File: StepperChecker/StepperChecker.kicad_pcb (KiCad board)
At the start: 2 copper layers, 89.4 x 69.1 mm, 31 parts, among them CN5 FEMALE_LEFT, CN6 FEMALE_RIGHT, J1 PJ-202AH, J10 CFG2, J11 CFG3, J12 Terminal, J2 Terminal, J3 FEATHER_A, J4 Molex SL, J5 JST-XH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

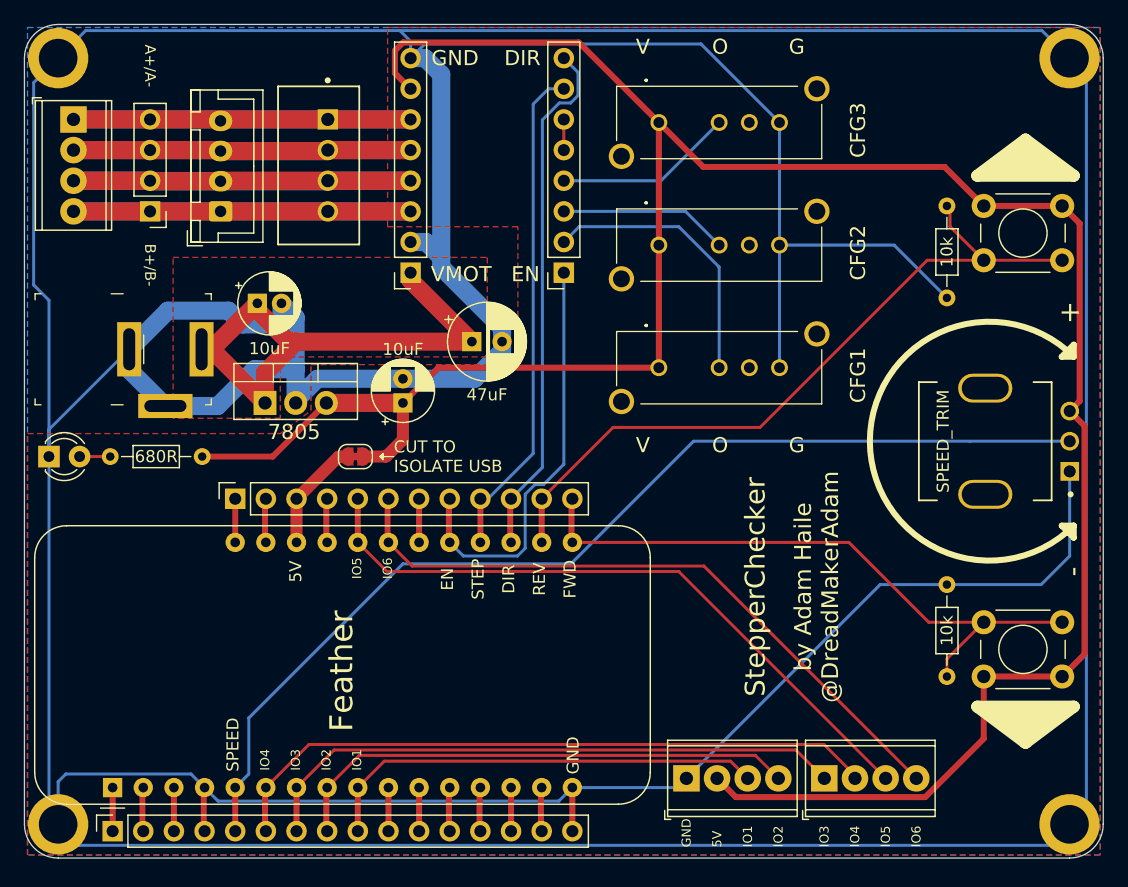
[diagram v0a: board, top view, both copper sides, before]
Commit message: Add Recom and jumpers
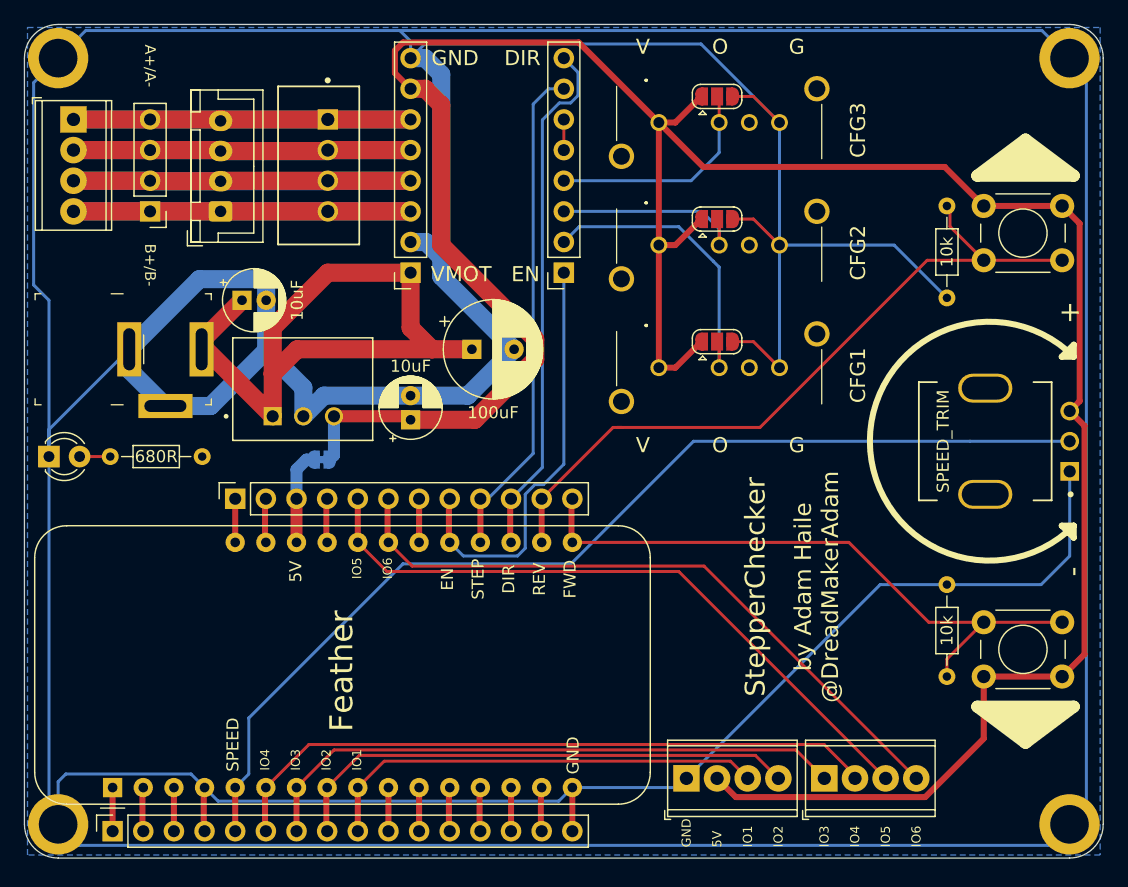
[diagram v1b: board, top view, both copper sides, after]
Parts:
- added JP1: CFG1, Jumper:SolderJumper-3_P1.3mm_Open_RoundedPad1.0x1.5mm, F.Cu at (152.4, 61.6)
- added JP3: CFG2, Jumper:SolderJumper-3_P1.3mm_Open_RoundedPad1.0x1.5mm, F.Cu at (152.4, 51.4)
- added JP4: CFG3, Jumper:SolderJumper-3_P1.3mm_Open_RoundedPad1.0x1.5mm, F.Cu at (152.4, 41.3)
- C3: value 47uF -> 100uF; footprint Capacitor_THT:CP_Radial_D6.3mm_P2.50mm -> Capacitor_THT:CP_Radial_D8.0mm_P3.50mm
- JP2: moved to B.Cu
- U2: value LM7805_TO220 -> R-78E5.0-1.0; footprint Package_TO_SOT_THT:TO-220-3_Vertical -> R-78E5.0-1:CONV_R-78E5.0-1.0
- moved U2 3.37 mm to (118.1, 65.5)
- moved JP2 2.81 mm to (119.6, 71.4)
- moved C2 1.53 mm to (127.0, 68.1)
- moved C1 1.30 mm to (113.0, 58.2)
- moved C3 0.63 mm to (132.1, 62.2)
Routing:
- net 5V: track 210.6 -> 226.1 mm
- net GND: track 589.0 -> 604.0 mm
- net VIN: track 45.9 -> 58.7 mm
- net /StepDriverX/CFG3: track 14.9 -> 18.6 mm
- net /StepDriverX/CFG2: track 14.0 -> 17.1 mm
- net /StepDriverX/CFG1: track 23.1 -> 25.4 mm
- net Net-(J8-Pad3): track 12.5 -> 11.0 mm
- removed copper zone on F.Cu, net 5V
- removed copper zone on F.Cu, net VIN
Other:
- board text removed: "7805"

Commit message: Fix missing traces and fill
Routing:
- net 5V: track 226.1 -> 240.0 mm
- added copper zone on F.Cu, net 5V
- added copper zone on F.Cu, net VIN
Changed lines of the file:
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@@
     (thickness 1.6)
     (drawings 99)
-    (tracks 306)
+    (tracks 309)
     (zones 0)
     (modules 34)
@@
   (page A4)
   (layers
-    (0 F.Cu signal)
-    (31 B.Cu signal)
+    (0 F.Cu signal hide)
+    (31 B.Cu signal hide)
     (32 B.Adhes user)
     (33 F.Adhes user)
@@
   (segment (start 148.941 63.754) (end 151.1 61.595) (width 0.5) (layer F.Cu) (net 2))
   (segment (start 147.574 63.754) (end 148.941 63.754) (width 0.5) (layer F.Cu) (net 2))
+  (segment (start 109.728 71.12) (end 120.015 71.12) (width 0.5) (layer F.Cu) (net 2))
+  (segment (start 120.65 70.485) (end 120.65 67.782) (width 0.5) (layer F.Cu) (net 2))
+  (segment (start 120.015 71.12) (end 120.65 70.485) (width 0.5) (layer F.Cu) (net 2))
   (segment (start 152.574 61.769) (end 152.4 61.595) (width 0.25) (layer F.Cu) (net 3))
   (segment (start 152.574 63.754) (end 152.574 61.769) (width 0.25) (layer F.Cu) (net 3))
@@
     (connect_pads (clearance 0.508))
     (min_thickness 0.254)
-    (fill (arc_segments 32) (thermal_gap 0.508) (thermal_bridge_width 0.508))
+    (fill yes (arc_segments 32) (thermal_gap 0.508) (thermal_bridge_width 0.508))
     (polygon
       (pts
@@
       )
     )
+  )
+  (zone (net 8) (net_name VIN) (layer F.Cu) (hatch edge 0.508)
+    (connect_pads (clearance 0.508))
+    (min_thickness 0.254)
+    (fill yes (arc_segments 32) (thermal_gap 0.508) (thermal_bridge_width 0.508))
+    (polygon
+      (pts
+        (xy 133.985 64.77) (xy 116.84 64.77) (xy 116.84 69.215) (xy 106.68 69.215) (xy 106.68 54.61)
+        (xy 133.985 54.61)
+      )
+    )
+  )
+  (zone (net 2) (net_name 5V) (layer F.Cu) (hatch edge 0.508)
+    (connect_pads (clearance 0.508))
+    (min_thickness 0.254)
+    (fill yes (arc_segments 32) (thermal_gap 0.508) (thermal_bridge_width 0.508))
+    (polygon
+      (pts
+        (xy 184.15 104.14) (xy 95.25 104.775) (xy 95.25 69.85) (xy 119.38 69.85) (xy 119.38 66.04)
+        (xy 135.255 66.04) (xy 135.255 53.34) (xy 124.46 53.34) (xy 124.46 35.56) (xy 184.15 35.56)
+      )
+    )

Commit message: updated labels
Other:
- board text added: "12-24V"
- board text added: "A+ A- B+ B-"
- board text added: "Choose One: R-78E5.0 TSR 1-2450 LM7805"
- board text added: "STEPSTICK"
- board text removed: "A+/A-"
- board text removed: "B+/B-"

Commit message: Minor board tweaks
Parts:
- JP2: value SolderJumper_2_Bridged -> SolderJumper_2_Open; footprint Jumper:SolderJumper-2_P1.3mm_Bridged_RoundedPad1.0x1.5mm -> Jumper:SolderJumper-2_P1.3mm_Open_RoundedPad1.0x1.5mm
- U2: footprint R-78E5.0-1:CONV_R-78E5.0-1.0 -> CONV_R-78E5.0-1.0
- moved J10 0.43 mm to (148.0, 53.6)
- moved J11 0.43 mm to (148.0, 43.4)
- moved J9 0.43 mm to (148.0, 63.8)
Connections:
- J3 pad 2: Net-(J3-Pad2) -> 3.3V
- U3 pad 2: Net-(J3-Pad2) -> 3.3V
- VR1 pad 3: 5V -> 3.3V
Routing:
- net 3.3V: track 0.00 -> 110.5 mm
- net 5V: track 240.0 -> 235.2 mm
- net Net-(J3-Pad2): track 3.64 -> 0.00 mm
- net GND: track 604.0 -> 605.9 mm
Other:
- board text added: "JUMP TO POWER FEATHER FROM ONBOARD 5V"
- board text removed: "CUT TO ISOLATE USB"
